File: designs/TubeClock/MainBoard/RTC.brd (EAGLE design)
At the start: 25.9 x 30 mm, 7 parts, among them IC1 DS1307N+, U1 S8411-45R, Y1 CM7V-T1A-32.768K-9PF-20PPM-TA-

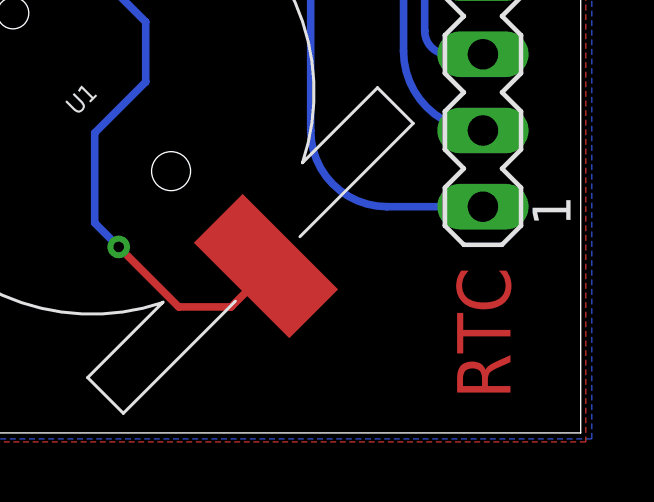
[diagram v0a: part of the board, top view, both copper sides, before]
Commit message: changed mainboard design radio
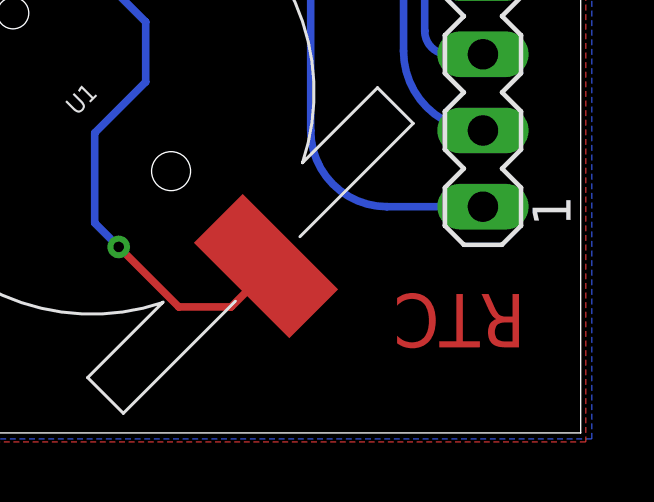
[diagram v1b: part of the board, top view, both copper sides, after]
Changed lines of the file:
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@@
 <drawing>
 <settings>
-<setting alwaysvectorfont="yes"/>
+<setting alwaysvectorfont="no"/>
 <setting verticaltext="up"/>
 </settings>
@@
 </layers>
 <board>
-<fusionsync huburn="a.cGVyc29uYWw6dWUyYTNmMDU1" projecturn="a.cGVyc29uYWw6dWUyYTNmMDU1IzIwMTgxMjEwMTY0OTQ5MjI2" f3durn="urn:adsk.wipprod:dm.lineage:2NRZY2egRq2a-97Lgq_41w" pcbguid="" lastpulledtime="" lastsyncedchangeguid="" latestrevisionid="be20785c-cd88-49c8-9540-4c2bb61ae9a5" lastsyncedrevisionid="be20785c-cd88-49c8-9540-4c2bb61ae9a5" lastboardhashguid="61ee3941-2d60-97d9-61af-c6b5881926df" lastpushedtime="2021-01-30T11:54:51Z" linktopcb3d="true"/>
+<fusionsync huburn="a.cGVyc29uYWw6dWUyYTNmMDU1" projecturn="a.cGVyc29uYWw6dWUyYTNmMDU1IzIwMTgxMjEwMTY0OTQ5MjI2" f3durn="urn:adsk.wipprod:dm.lineage:2NRZY2egRq2a-97Lgq_41w" pcbguid="" lastpulledtime="" lastsyncedchangeguid="" latestrevisionid="00457b39-1cc4-4e0d-8cc4-575e2a4fb573" lastsyncedrevisionid="00457b39-1cc4-4e0d-8cc4-575e2a4fb573" lastboardhashguid="dc495cea-6761-ddff-0404-1ea1a227fa8d" lastpushedtime="2021-02-01T17:07:03Z" linktopcb3d="true"/>
 <plain>
 <wire x1="25.899815625" y1="-0.000321875" x2="25.899815625" y2="27.052746875" width="0" layer="20"/>
@@
 <wire x1="-0.000184375" y1="-0.000321875" x2="25.899815625" y2="-0.000321875" width="0" layer="20"/>
 <hole x="22.9" y="25.9" drill="2.8"/>
-<text x="23.558184375" y="1.130321875" size="1.778" layer="29" font="vector" ratio="20" rot="SR90">RTC</text>
-<text x="23.558184375" y="1.130321875" size="1.778" layer="1" font="vector" ratio="20" rot="SR90">RTC</text>
+<text x="24.058184375" y="4.630321875" size="1.778" layer="29" font="vector" ratio="20" rot="SR180">RTC</text>
+<text x="24.058184375" y="4.630321875" size="1.778" layer="1" font="vector" ratio="20" rot="SR180">RTC</text>
 </plain>
 <attributes>
